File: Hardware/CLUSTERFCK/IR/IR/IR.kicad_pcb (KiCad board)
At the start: 2 copper layers, 142 x 72.4 mm, 40 parts, among them J1 Conn_02x20_Counter_Clockwise, J2 Conn_02x20_Counter_Clockwise, U1 74LS08, U2 74HCT574, U3 74HCT574

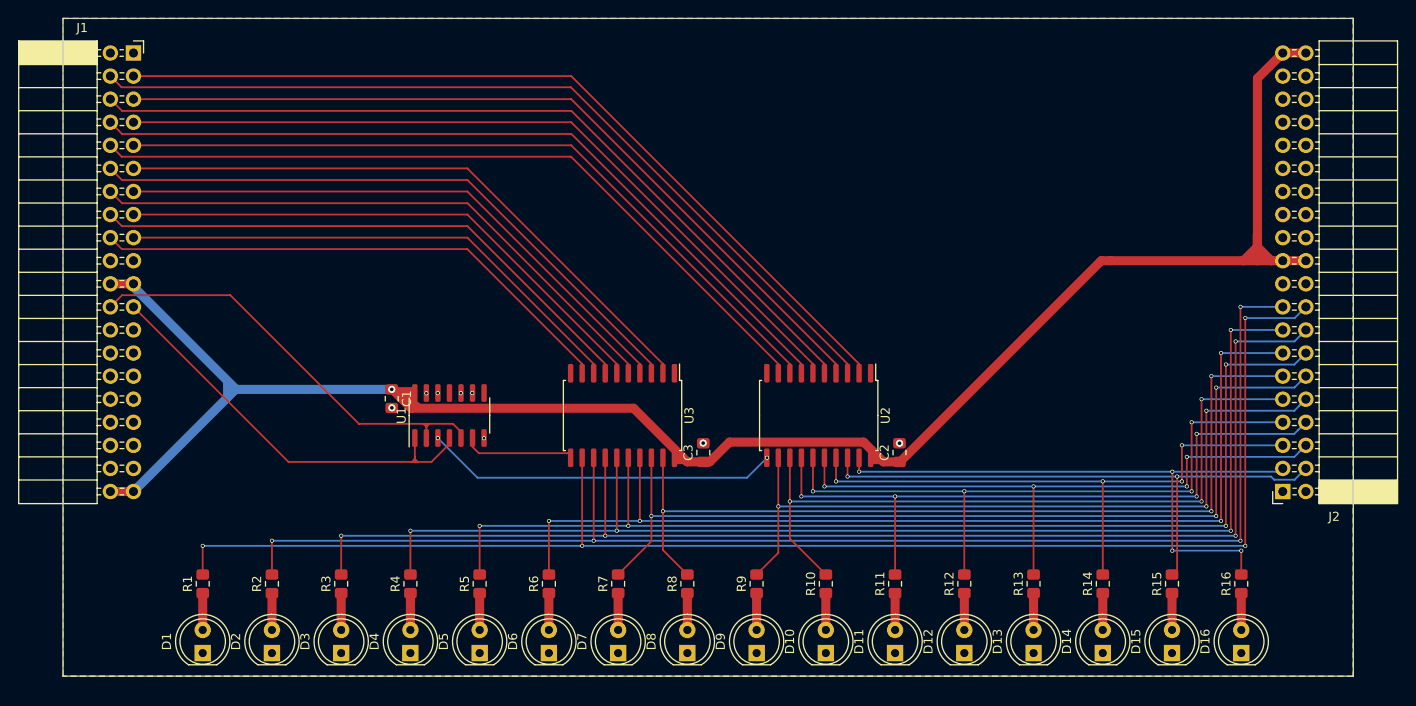
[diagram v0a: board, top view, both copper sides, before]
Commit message: quickfix IR groundplane connections
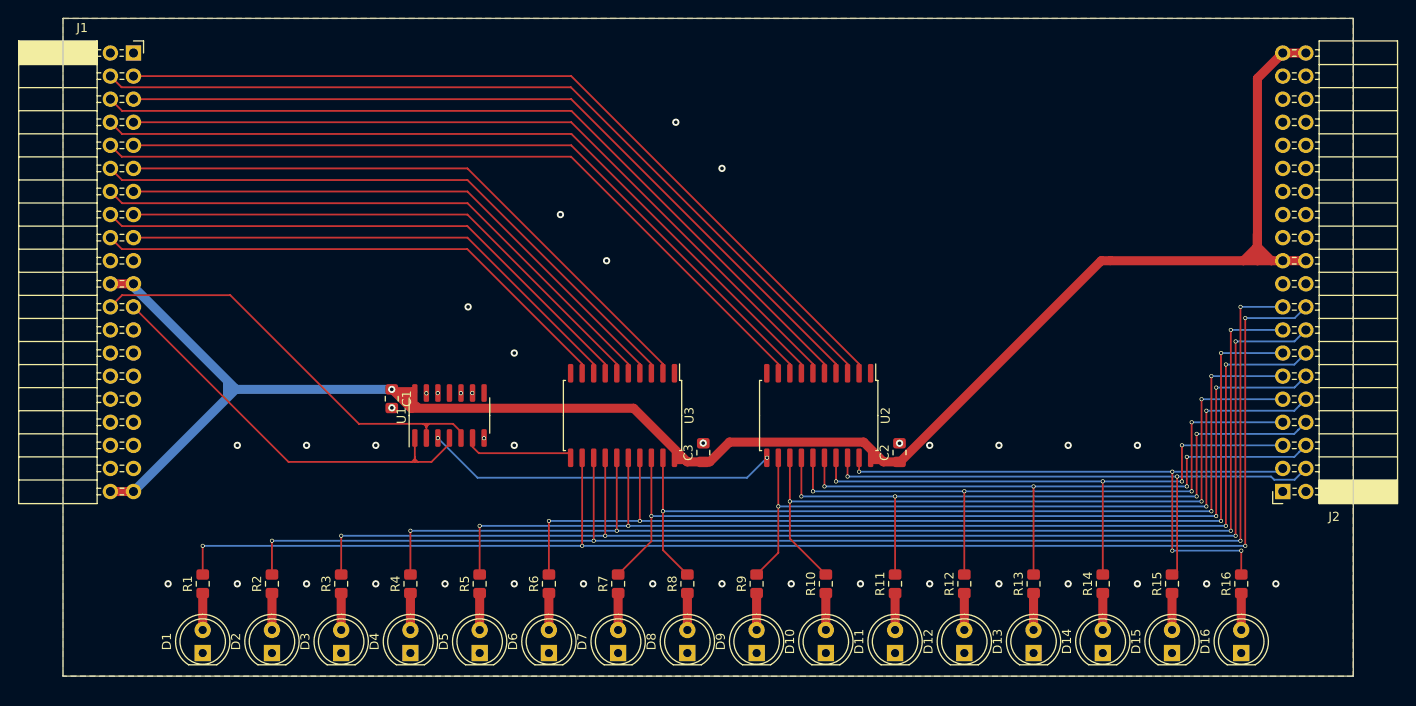
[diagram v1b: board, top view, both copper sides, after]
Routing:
- net GND: vias 8 -> 39
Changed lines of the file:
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@@
     (thickness 1.6)
     (drawings 8)
-    (tracks 346)
+    (tracks 377)
     (modules 40)
     (nets 55)
@@
       (dielectric_constraints no)
     )
-    (last_trace_width 0.25)
+    (last_trace_width 1)
     (user_trace_width 0.2)
     (user_trace_width 0.5)
@@
   (gr_line (start 112.894 182.88) (end 254.894 182.88) (layer "Edge.Cuts") (width 0.05))
   (gr_line (start 112.894 110.49) (end 254.894 110.49) (layer "Edge.Cuts") (width 0.05))
+  (via (at 162.56 147.32) (size 0.8) (drill 0.4) (layers "F.Cu" "B.Cu") (net 1))
+  (via (at 157.48 142.24) (size 0.8) (drill 0.4) (layers "F.Cu" "B.Cu") (net 1))
+  (via (at 185.42 127) (size 0.8) (drill 0.4) (layers "F.Cu" "B.Cu") (net 1))
+  (via (at 180.34 121.92) (size 0.8) (drill 0.4) (layers "F.Cu" "B.Cu") (net 1))
+  (via (at 172.72 137.16) (size 0.8) (drill 0.4) (layers "F.Cu" "B.Cu") (net 1))
+  (via (at 167.64 132.08) (size 0.8) (drill 0.4) (layers "F.Cu" "B.Cu") (net 1))
+  (via (at 132.08 157.48) (size 0.8) (drill 0.4) (layers "F.Cu" "B.Cu") (net 1))
+  (via (at 139.7 157.48) (size 0.8) (drill 0.4) (layers "F.Cu" "B.Cu") (net 1))
+  (via (at 147.32 157.48) (size 0.8) (drill 0.4) (layers "F.Cu" "B.Cu") (net 1))
+  (via (at 162.56 157.48) (size 0.8) (drill 0.4) (layers "F.Cu" "B.Cu") (net 1))
+  (via (at 231.14 157.48) (size 0.8) (drill 0.4) (layers "F.Cu" "B.Cu") (net 1))
+  (via (at 208.28 157.48) (size 0.8) (drill 0.4) (layers "F.Cu" "B.Cu") (net 1))
+  (via (at 215.9 157.48) (size 0.8) (drill 0.4) (layers "F.Cu" "B.Cu") (net 1))
+  (via (at 223.52 157.48) (size 0.8) (drill 0.4) (layers "F.Cu" "B.Cu") (net 1))
+  (via (at 246.38 172.72) (size 0.8) (drill 0.4) (layers "F.Cu" "B.Cu") (net 1))
+  (via (at 238.76 172.72) (size 0.8) (drill 0.4) (layers "F.Cu" "B.Cu") (net 1))
+  (via (at 231.14 172.72) (size 0.8) (drill 0.4) (layers "F.Cu" "B.Cu") (net 1))
+  (via (at 223.52 172.72) (size 0.8) (drill 0.4) (layers "F.Cu" "B.Cu") (net 1))
+  (via (at 215.9 172.72) (size 0.8) (drill 0.4) (layers "F.Cu" "B.Cu") (net 1))
+  (via (at 208.28 172.72) (size 0.8) (drill 0.4) (layers "F.Cu" "B.Cu") (net 1))
+  (via (at 200.66 172.72) (size 0.8) (drill 0.4) (layers "F.Cu" "B.Cu") (net 1))
+  (via (at 193.04 172.72) (size 0.8) (drill 0.4) (layers "F.Cu" "B.Cu") (net 1))
+  (via (at 185.42 172.72) (size 0.8) (drill 0.4) (layers "F.Cu" "B.Cu") (net 1))
+  (via (at 177.8 172.72) (size 0.8) (drill 0.4) (layers "F.Cu" "B.Cu") (net 1))
+  (via (at 170.18 172.72) (size 0.8) (drill 0.4) (layers "F.Cu" "B.Cu") (net 1))
+  (via (at 162.56 172.72) (size 0.8) (drill 0.4) (layers "F.Cu" "B.Cu") (net 1))
+  (via (at 154.94 172.72) (size 0.8) (drill 0.4) (layers "F.Cu" "B.Cu") (net 1))
+  (via (at 147.32 172.72) (size 0.8) (drill 0.4) (layers "F.Cu" "B.Cu") (net 1))
+  (via (at 139.7 172.72) (size 0.8) (drill 0.4) (layers "F.Cu" "B.Cu") (net 1))
+  (via (at 132.08 172.72) (size 0.8) (drill 0.4) (layers "F.Cu" "B.Cu") (net 1))
+  (via (at 124.46 172.72) (size 0.8) (drill 0.4) (layers "F.Cu" "B.Cu") (net 1))
   (segment (start 247.14 142.24) (end 247.33 142.24) (width 0.25) (layer "B.Cu") (net 21))
   (segment (start 242.81 137.16) (end 228.16 137.16) (width 1) (layer "F.Cu") (net 2))

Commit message: 0044 | 0,2 | Review IR by Leon
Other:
- board size 142 x 72.4 mm -> 142 x 73.7 mm
- board text added: "Instruction Register"
- board text added: "Kevin da Silva Fernandes 2020"
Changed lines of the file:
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@@
   (general
     (thickness 1.6)
-    (drawings 8)
+    (drawings 12)
     (tracks 377)
     (modules 40)
@@
       (dielectric_constraints no)
     )
-    (last_trace_width 1)
+    (last_trace_width 0.25)
     (user_trace_width 0.2)
     (user_trace_width 0.5)
@@
     (tags "SOIC SO")
     (attr smd)
-    (fp_text reference "U1" (at 0 -5.28 90) (layer "F.SilkS")
+    (fp_text reference "U1" (at -0.035 5.565 90) (layer "F.SilkS")
       (effects (font (size 1 1) (thickness 0.15)))
     )
@@
     (tags "capacitor handsolder")
     (attr smd)
-    (fp_text reference "C3" (at 0 -1.65 90) (layer "F.SilkS")
+    (fp_text reference "C3" (at -0.005 1.745 90) (layer "F.SilkS")
       (effects (font (size 1 1) (thickness 0.15)))
     )
@@
     (tags "capacitor handsolder")
     (attr smd)
-    (fp_text reference "C2" (at 0 -1.65 90) (layer "F.SilkS")
+    (fp_text reference "C2" (at -0.045 1.795 90) (layer "F.SilkS")
       (effects (font (size 1 1) (thickness 0.15)))
     )
@@
     (tags "capacitor handsolder")
     (attr smd)
-    (fp_text reference "C1" (at 0 -1.65 90) (layer "F.SilkS")
+    (fp_text reference "C1" (at 0.015 1.645 90) (layer "F.SilkS")
       (effects (font (size 1 1) (thickness 0.15)))
     )
@@
     )
   )
+  (gr_text "Kevin da Silva Fernandes 2020" (at 218.27 120.91) (layer "F.SilkS")
+    (effects (font (size 2 2) (thickness 0.3)))
+  )
+  (gr_line (start 254.894 182.88) (end 254.894 184.15) (layer "Edge.Cuts") (width 0.05))
+  (gr_line (start 112.894 182.88) (end 112.894 184.15) (layer "Edge.Cuts") (width 0.05))
+  (gr_text "Instruction Register" (at 219.59 115.53) (layer "F.SilkS")
+    (effects (font (size 3 3) (thickness 0.75)))
+  )
   (gr_poly (pts (xy 131.48 151.28) (xy 130.56 152.07) (xy 130.56 150.38)) (layer "B.Cu") (width 0.1))
   (gr_poly (pts (xy 180.99 159.09) (xy 180.27 159.17) (xy 180.53 158.55)) (layer "F.Cu") (width 0.1))
@@
   (gr_line (start 254.894 110.49) (end 254.894 182.88) (layer "Edge.Cuts") (width 0.05))
   (gr_line (start 112.894 182.88) (end 112.894 110.49) (layer "Edge.Cuts") (width 0.05))
-  (gr_line (start 112.894 182.88) (end 254.894 182.88) (layer "Edge.Cuts") (width 0.05))
+  (gr_line (start 112.894 184.15) (end 254.894 184.15) (layer "Edge.Cuts") (width 0.05))
   (gr_line (start 112.894 110.49) (end 254.894 110.49) (layer "Edge.Cuts") (width 0.05))
   (via (at 162.56 147.32) (size 0.8) (drill 0.4) (layers "F.Cu" "B.Cu") (net 1))
@@
     (polygon
       (pts
-        (xy 254.89 182.88) (xy 112.9 182.87) (xy 112.89 110.49) (xy 254.89 110.49)
+        (xy 254.9 184.15) (xy 112.91 184.15) (xy 112.9 110.49) (xy 254.9 110.49)
       )
     )

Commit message: 0065 | 24h | ADDR & DATA & PLACEHOLDER etc
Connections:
- J1 pad 10: MEM7 -> (no net)
- J1 pad 11: MEM8 -> (no net)
- J1 pad 12: MEM9 -> (no net)
- J1 pad 13: MEM10 -> (no net)
- J1 pad 14: MEM11 -> (no net)
- J1 pad 15: MEM12 -> (no net)
- J1 pad 16: MEM13 -> (no net)
- J1 pad 17: MEM14 -> CLK
- J1 pad 18: MEM15 -> II
- J1 pad 23: CLK -> ARG0
- J1 pad 24: II -> ARG1
- J1 pad 25: (no net) -> ARG2
- J1 pad 26: (no net) -> ARG3
- J1 pad 27: (no net) -> ARG4
- J1 pad 28: (no net) -> ARG5
- J1 pad 29: (no net) -> ARG6
- J1 pad 3: MEM0 -> (no net)
- J1 pad 30: (no net) -> ARG7
- J1 pad 31: (no net) -> ARG8
- J1 pad 32: (no net) -> ARG9
- J1 pad 33: (no net) -> ARG10
- J1 pad 34: (no net) -> ARG11
- J1 pad 35: (no net) -> OP0
- J1 pad 36: (no net) -> OP1
- J1 pad 37: (no net) -> OP2
- J1 pad 38: (no net) -> OP3
- J1 pad 4: MEM1 -> (no net)
- J1 pad 5: MEM2 -> (no net)
- J1 pad 6: MEM3 -> (no net)
- J1 pad 7: MEM4 -> (no net)
- J1 pad 8: MEM5 -> (no net)
- J1 pad 9: MEM6 -> (no net)
- J2 pad 10: ARG7 -> (no net)
- J2 pad 11: ARG8 -> (no net)
- J2 pad 12: ARG9 -> (no net)
- J2 pad 13: ARG10 -> (no net)
- J2 pad 14: ARG11 -> (no net)
- J2 pad 15: OP0 -> (no net)
- J2 pad 16: OP1 -> (no net)
- J2 pad 17: OP2 -> (no net)
- J2 pad 18: OP3 -> (no net)
- J2 pad 23: (no net) -> MEM0
- J2 pad 24: (no net) -> MEM1
- J2 pad 25: (no net) -> MEM2
- J2 pad 26: (no net) -> MEM3
- J2 pad 27: (no net) -> MEM4
- J2 pad 28: (no net) -> MEM5
- J2 pad 29: (no net) -> MEM6
- J2 pad 3: ARG0 -> (no net)
- J2 pad 30: (no net) -> MEM7
- J2 pad 31: (no net) -> MEM8
- J2 pad 32: (no net) -> MEM9
- J2 pad 33: (no net) -> MEM10
- J2 pad 34: (no net) -> MEM11
- J2 pad 35: (no net) -> MEM12
- J2 pad 36: (no net) -> MEM13
- J2 pad 37: (no net) -> MEM14
- J2 pad 38: (no net) -> MEM15
- J2 pad 4: ARG1 -> (no net)
- J2 pad 5: ARG2 -> (no net)
- J2 pad 6: ARG3 -> (no net)
- J2 pad 7: ARG4 -> (no net)
- J2 pad 8: ARG5 -> (no net)
- J2 pad 9: ARG6 -> (no net)
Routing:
- net OP3: track 159.9 -> 68.3 mm, vias 4 -> 2
- net OP2: track 150.0 -> 66.8 mm, vias 4 -> 2
- net ARG0: track 67.3 -> 142.3 mm, vias 4 -> 3
- net ARG1: track 64.3 -> 138.1 mm, vias 2 -> 3
- net OP1: track 141.0 -> 71.4 mm, vias 4 -> 2
- net OP0: track 131.0 -> 69.9 mm, vias 4 -> 2
- net ARG2: track 66.0 -> 126.4 mm, vias 4 -> 3
- net ARG3: track 69.6 -> 121.6 mm, vias 4 -> 3
- net ARG11: track 122.1 -> 74.6 mm, vias 4 -> 2
- net MEM0: track 94.0 -> 53.4 mm
- net ARG10: track 112.1 -> 73.1 mm, vias 4 -> 2
- net ARG4: track 72.2 -> 110.6 mm, vias 4 -> 3
- net MEM1: track 95.3 -> 58.2 mm
- net MEM15: track 58.7 -> 94.7 mm
- net MEM2: track 90.4 -> 57.0 mm
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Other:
- net class Default removed

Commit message: 0066 | 6h | made holes in pcbs
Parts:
- added REF**: MountingHole_4.3mm_M4, MountingHole:MountingHole_4.3mm_M4, F.Cu at (240.4, 143.3)
- added REF**: MountingHole_4.3mm_M4, MountingHole:MountingHole_4.3mm_M4, F.Cu at (127.0, 115.7)
- added REF**: MountingHole_4.3mm_M4, MountingHole:MountingHole_4.3mm_M4, F.Cu at (249.2, 169.6)
- added REF**: MountingHole_4.3mm_M4, MountingHole:MountingHole_4.3mm_M4, F.Cu at (118.1, 178.9)
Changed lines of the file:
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@@
     )
+  )
+  (footprint "MountingHole:MountingHole_4.3mm_M4" (layer "F.Cu")
+    (at 240.4 143.29)
+    (descr "Mounting Hole 4.3mm, no annular, M4")
+    (tags "mounting hole 4.3mm no annular m4")
+    (attr exclude_from_pos_files exclude_from_bom)
+    (fp_text reference "REF**" (at -0.04 -3.25) (layer "F.SilkS")
+      (effects (font (size 1 1) (thickness 0.15)))
+    )
+    (fp_text value "MountingHole_4.3mm_M4" (at 0 5.3) (layer "F.Fab")
+      (effects (font (size 1 1) (thickness 0.15)))
+    )
+    (fp_text user "${REFERENCE}" (at 0.3 0) (layer "F.Fab")
+      (effects (font (size 1 1) (thickness 0.15)))
+    )
+    (fp_circle (center 0 0) (end 4.3 0) (layer "Cmts.User") (width 0.15) (fill none))
+    (fp_circle (center 0 0) (end 4.55 0) (layer "F.CrtYd") (width 0.05) (fill none))
+    (pad "1" np_thru_hole circle (at 0 0) (size 4.3 4.3) (drill 4.3) (layers *.Cu *.Mask))
   )
   (footprint "Resistor_SMD:R_0805_2012Metric_Pad1.15x1.40mm_HandSolder" (layer "F.Cu")
@@
       (rotate (xyz 0 0 0))
     )
+  )
+  (footprint "MountingHole:MountingHole_4.3mm_M4" (layer "F.Cu")
+    (at 126.98 115.71)
+    (descr "Mounting Hole 4.3mm, no annular, M4")
+    (tags "mounting hole 4.3mm no annular m4")
+    (attr exclude_from_pos_files exclude_from_bom)
+    (fp_text reference "REF**" (at -0.04 -3.25) (layer "F.SilkS")
+      (effects (font (size 1 1) (thickness 0.15)))
+    )
+    (fp_text value "MountingHole_4.3mm_M4" (at 0 5.3) (layer "F.Fab")
+      (effects (font (size 1 1) (thickness 0.15)))
+    )
+    (fp_text user "${REFERENCE}" (at 0.3 0) (layer "F.Fab")
+      (effects (font (size 1 1) (thickness 0.15)))
+    )
+    (fp_circle (center 0 0) (end 4.3 0) (layer "Cmts.User") (width 0.15) (fill none))
+    (fp_circle (center 0 0) (end 4.55 0) (layer "F.CrtYd") (width 0.05) (fill none))
+    (pad "1" np_thru_hole circle (at 0 0) (size 4.3 4.3) (drill 4.3) (layers *.Cu *.Mask))
   )
   (footprint "LED_THT:LED_D5.0mm" (layer "F.Cu")
@@
     )
   )
+  (footprint "MountingHole:MountingHole_4.3mm_M4" (layer "F.Cu")
+    (at 249.15 169.6)
+    (descr "Mounting Hole 4.3mm, no annular, M4")
+    (tags "mounting hole 4.3mm no annular m4")
+    (attr exclude_from_pos_files exclude_from_bom)
+    (fp_text reference "REF**" (at -0.04 -3.25) (layer "F.SilkS")
+      (effects (font (size 1 1) (thickness 0.15)))
+    )
+    (fp_text value "MountingHole_4.3mm_M4" (at 0 5.3) (layer "F.Fab")
+      (effects (font (size 1 1) (thickness 0.15)))
+    )
+    (fp_text user "${REFERENCE}" (at 0.3 0) (layer "F.Fab")
+      (effects (font (size 1 1) (thickness 0.15)))
+    )
+    (fp_circle (center 0 0) (end 4.3 0) (layer "Cmts.User") (width 0.15) (fill none))
+    (fp_circle (center 0 0) (end 4.55 0) (layer "F.CrtYd") (width 0.05) (fill none))
+    (pad "1" np_thru_hole circle (at 0 0) (size 4.3 4.3) (drill 4.3) (layers *.Cu *.Mask))
+  )
   (footprint "Capacitor_SMD:C_0805_2012Metric_Pad1.15x1.40mm_HandSolder" (layer "F.Cu")
     (at 183.365 158.275 90)
@@
       (rotate (xyz 0 0 0))
     )
+  )
+  (footprint "MountingHole:MountingHole_4.3mm_M4" (layer "F.Cu")
+    (at 118.11 178.89)
+    (descr "Mounting Hole 4.3mm, no annular, M4")
+    (tags "mounting hole 4.3mm no annular m4")
+    (attr exclude_from_pos_files exclude_from_bom)
+    (fp_text reference "REF**" (at -0.04 -3.25) (layer "F.SilkS")
+      (effects (font (size 1 1) (thickness 0.15)))
+    )
+    (fp_text value "MountingHole_4.3mm_M4" (at 0 5.3) (layer "F.Fab")
+      (effects (font (size 1 1) (thickness 0.15)))
+    )
+    (fp_text user "${REFERENCE}" (at 0.3 0) (layer "F.Fab")
+      (effects (font (size 1 1) (thickness 0.15)))
+    )
+    (fp_circle (center 0 0) (end 4.3 0) (layer "Cmts.User") (width 0.15) (fill none))
+    (fp_circle (center 0 0) (end 4.55 0) (layer "F.CrtYd") (width 0.05) (fill none))
+    (pad "1" np_thru_hole circle (at 0 0) (size 4.3 4.3) (drill 4.3) (layers *.Cu *.Mask))
   )
   (footprint "Resistor_SMD:R_0805_2012Metric_Pad1.15x1.40mm_HandSolder" (layer "F.Cu")
@@
   (via (at 209.39 147.31) (size 0.8) (drill 0.4) (layers "F.Cu" "B.Cu") (net 1))
   (via (at 231.14 172.72) (size 0.8) (drill 0.4) (layers "F.Cu" "B.Cu") (net 1))
-  (via (at 246.38 172.72) (size 0.8) (drill 0.4) (layers "F.Cu" "B.Cu") (net 1))
+  (via (at 244.05 167.35) (size 0.8) (drill 0.4) (layers "F.Cu" "B.Cu") (net 1))
   (via (at 183.35 157.23) (size 0.8) (drill 0.4) (layers "F.Cu" "B.Cu") (net 1))
   (via (at 191.46 122.69) (size 0.8) (drill 0.4) (layers "F.Cu" "B.Cu") (net 1))
